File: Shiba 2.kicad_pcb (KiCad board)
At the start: 2 copper layers, 85.7 x 54 mm, 40 parts, among them J1 Conn_01x04_Pin, U1 STM32F072C8Tx, U3 AP62150Z6, U5 MIC5504-3.3YM5

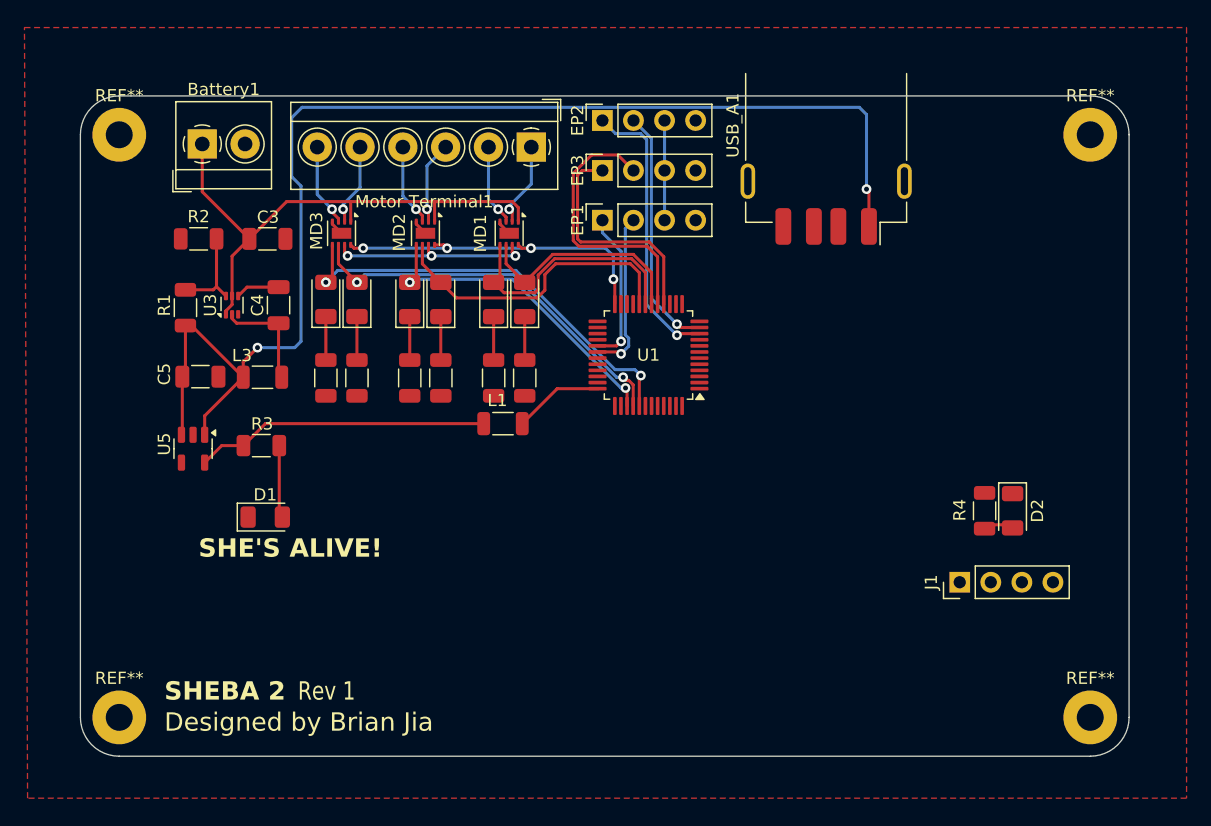
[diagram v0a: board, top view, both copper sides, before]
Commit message: About ready to order but I realized I used underpowered motor drivers
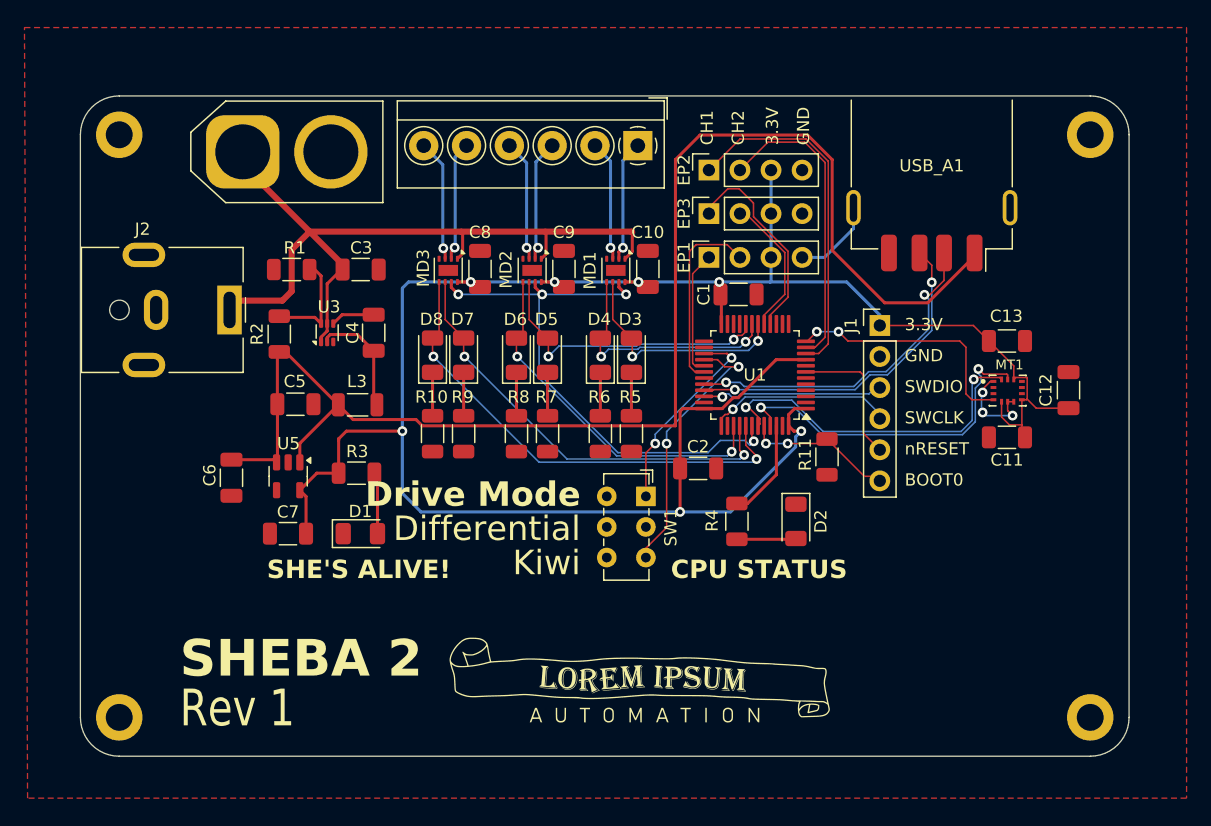
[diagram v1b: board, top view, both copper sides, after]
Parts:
- removed L1: L100nH, Inductor_SMD:L_1206_3216Metric
- removed REF** (x4): MountingHole_2.2mm_M2_Pad, MountingHole:MountingHole_2.2mm_M2_Pad
- added C1: C_Small22uF, Capacitor_SMD:C_1206_3216Metric, F.Cu at (107.1, 46.2)
- added C10: C_Small1uF, Capacitor_SMD:C_1206_3216Metric, F.Cu at (99.7, 44.1)
- added C11: C_Small2.2uF, Capacitor_SMD:C_1206_3216Metric, F.Cu at (129.1, 57.9)
- added C12: C_Small0.1uF, Capacitor_SMD:C_1206_3216Metric, F.Cu at (134.1, 54.0)
- added C13: C_Small10nF, Capacitor_SMD:C_1206_3216Metric, F.Cu at (129.1, 50.0)
- added C2: C_Small22uF, Capacitor_SMD:C_1206_3216Metric, F.Cu at (103.8, 60.4)
- added C6: C1uF, Capacitor_SMD:C_1206_3216Metric, F.Cu at (65.7, 61.2)
- added C7: C1uF, Capacitor_SMD:C_1206_3216Metric, F.Cu at (70.3, 65.8)
- added C8: C_Small1uF, Capacitor_SMD:C_1206_3216Metric, F.Cu at (86.0, 44.1)
- added C9: C_Small1uF, Capacitor_SMD:C_1206_3216Metric, F.Cu at (92.9, 44.1)
- added G***: LOGO, Library:lorem-ipsum-logo, F.Cu at (99.0, 79.9)
- added G***: LOGO, Library:lorem-ipsum-insignia, F.Cu at (124.2, 72.4)
- added H1: MountingHole_Pad, MountingHole:MountingHole_2.2mm_M2_DIN965_Pad, F.Cu at (56.5, 33.1)
- added H2: MountingHole_Pad, MountingHole:MountingHole_2.2mm_M2_DIN965_Pad, F.Cu at (135.9, 33.1)
- added H3: MountingHole_Pad, MountingHole:MountingHole_2.2mm_M2_DIN965_Pad, F.Cu at (56.5, 80.8)
- added H4: MountingHole_Pad, MountingHole:MountingHole_2.2mm_M2_DIN965_Pad, F.Cu at (135.9, 80.8)
- added J2: Jack-DC, Connector_BarrelJack:BarrelJack_CUI_PJ-063AH_Horizontal, F.Cu at (65.5, 47.5)
- added MT1: ICM-42670-P, Library:XDCR_ICM-42670-P, F.Cu at (129.1, 54.1)
- added R11: 10k, Resistor_SMD:R_1206_3216Metric, F.Cu at (114.4, 59.5)
- added SW1: SW_SPDT, Button_Switch_THT:SW_E-Switch_EG1271_SPDT, F.Cu at (99.6, 62.7)
- Battery1: footprint TerminalBlock_4Ucon:TerminalBlock_4Ucon_1x02_P3.50mm_Horizontal -> Connector_AMASS:AMASS_XT60-F_1x02_P7.20mm_Vertical
- C3: value C_Small10uF -> C10uF
- C4: value C_Small100nF -> C0.1uF
- C5: value C_Small22uF -> C22uF
- D1, D2, D3, D5, D7: value LED -> LED Green
- D4, D6, D8: value LED -> LED Red
- J1: value Conn_01x04_Pin -> Conn_01x06_Pin; footprint Connector_PinHeader_2.54mm:PinHeader_1x04_P2.54mm_Vertical -> Connector_PinHeader_2.54mm:PinHeader_1x06_P2.54mm_Vertical
- moved J1 22.0 mm to (118.7, 48.7), turned to 0 degrees
- moved R4 20.3 mm to (107.0, 64.8)
- moved D2 17.7 mm to (111.8, 64.8)
- moved R2 10.2 mm to (69.6, 49.4), turned to 90 degrees
- moved D6 9.84 mm to (89.0, 51.2)
- moved D7 9.84 mm to (84.7, 51.2)
- moved R8 9.84 mm to (89.0, 57.6)
- moved R9 9.84 mm to (84.7, 57.6)
- moved D3 9.84 mm to (98.4, 51.2)
- moved D4 9.84 mm to (95.8, 51.2)
- moved D5 9.84 mm to (91.5, 51.2)
- moved D8 9.84 mm to (82.1, 51.2)
- moved R10 9.84 mm to (82.1, 57.6)
- moved R5 9.84 mm to (98.4, 57.6)
- moved R6 9.84 mm to (95.8, 57.6)
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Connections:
- net SYS_JTCK-SWCLK renamed SYS_SWCLK
- net SYS_JTMS-SWDIO renamed SYS_SWDIO
- R1 pad 2: +5V -> GND
- R2 pad 1: GND -> +5V
- U1 pad 12: unconnected-(U1-PA2-Pad12) -> IMU_INT
- U1 pad 2: M_SLEEP -> unconnected-(U1-PC13-Pad2)
- U1 pad 22: BLINKY -> unconnected-(U1-PB11-Pad22)
- U1 pad 27: unconnected-(U1-PB14-Pad27) -> DIFFERENTIAL_DRIVE
- U1 pad 28: unconnected-(U1-PB15-Pad28) -> KIWI_DRIVE
- U1 pad 36: Net-(U1-VDDA) -> +3V3
- U1 pad 42: unconnected-(U1-PB6-Pad42) -> M_SLEEP
- U1 pad 43: unconnected-(U1-PB7-Pad43) -> I2C1_SDA
- U1 pad 44: GND -> BOOT0
- U1 pad 45: unconnected-(U1-PB8-Pad45) -> IC21_SCL
- U1 pad 46: unconnected-(U1-PB9-Pad46) -> BLINKY
- U1 pad 7: GND -> NRST
- U1 pad 9: Net-(U1-VDDA) -> +3V3
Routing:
- net +3V3: track 60.6 -> 176.1 mm, vias 4 -> 7
- net M_SLEEP: track 16.7 -> 46.3 mm, vias 3 -> 4
- net IC21_SCL: track 0.00 -> 28.5 mm, vias 0 -> 2
- net I2C1_SDA: track 0.00 -> 28.2 mm, vias 0 -> 2
- net /USB_DM: track 0.00 -> 27.8 mm, vias 0 -> 2
- net /USB_DP: track 0.00 -> 27.4 mm, vias 0 -> 2
- net KIWI_DRIVE: track 0.00 -> 21.4 mm, vias 0 -> 2
- net IMU_INT: track 0.00 -> 20.2 mm, vias 0 -> 2
- net +BATT: track 44.2 -> 63.3 mm
- net DIFFERENTIAL_DRIVE: track 0.00 -> 15.9 mm, vias 0 -> 2
- net SYS_SWDIO: track 0.00 -> 15.1 mm, vias 0 -> 1
- net SYS_SWCLK: track 0.00 -> 14.9 mm, vias 0 -> 1
- net BOOT0: track 0.00 -> 12.2 mm, vias 0 -> 2
- net NRST: track 0.00 -> 11.5 mm
- net TIM3_CH2: track 22.9 -> 11.7 mm
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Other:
- board text added: "3.3V"
- board text added: "BOOT0"
- board text added: "CH1"
- board text added: "CH2"
- board text added: "CPU STATUS"
- board text added: "Designed by Brian Jia Wouldn't be possible without: Griffin Bohm Sam Patterson Drew Straub"
- board text added: "Differential"
- board text added: "Drive Mode"
- board text added: "GND"
- board text added: "Kiwi"
- board text added: "SWCLK"
- board text added: "SWDIO"
- board text added: "nRESET"
- board text removed: "Designed by Brian Jia"

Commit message: REV 1 ORDERED WOOOOO
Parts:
- removed C9: C_Small1uF, Capacitor_SMD:C_1206_3216Metric
- added C15: C1uF, Capacitor_SMD:C_1206_3216Metric, F.Cu at (92.0, 46.0)
- added G***: LOGO, LOGO, F.Cu at (103.4, 74.9)
- added J3: Conn_01x010_Pin, Connector_PinSocket_2.54mm:PinSocket_1x10_P2.54mm_Vertical, F.Cu at (135.4, 38.9)
- added R12: R10k, Resistor_SMD:R_1206_3216Metric, F.Cu at (115.1, 65.5)
- added R13: R10k, Resistor_SMD:R_1206_3216Metric, F.Cu at (120.1, 65.5)
- C10, C8: value C_Small1uF -> C1uF
- MD1, MD2, MD3: value DRV8837C -> ZXBM5210-S; footprint Package_SON:WSON-8-1EP_2x2mm_P0.5mm_EP0.9x1.6mm -> Package_SO:SOIC-8_3.9x4.9mm_P1.27mm
- moved MD1 14.8 mm to (82.5, 41.5), turned to 0 degrees
- moved MD3 14.7 mm to (97.9, 41.5), turned to 0 degrees
- moved C12 8.52 mm to (128.8, 60.7), turned to 180 degrees
- moved D2 3.37 mm to (108.5, 64.8)
- moved MD2 2.71 mm to (90.2, 41.5), turned to 0 degrees
- moved G*** 2.51 mm to (126.0, 74.2)
- moved R11 2.31 mm to (112.8, 61.2)
- moved R4 2.10 mm to (104.9, 64.8)
- moved C10 2.05 mm to (98.9, 46.0), turned to 0 degrees
- moved C8 2.05 mm to (85.1, 46.0), turned to 0 degrees
- moved G*** 2.03 mm to (101.1, 79.9)
- moved C1 0.30 mm to (107.4, 46.2)
- moved C13 0.26 mm to (128.8, 50.0)
- moved C11 0.25 mm to (128.8, 57.9)
- renumbered U3 to U1, U5 to U2, U1 to U3
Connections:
- D4 pad 2: M1_BACK -> M1_REV
- D6 pad 2: M2_BACK -> M2_REV
- D8 pad 2: M3_BACK -> M3_REV
- MD1 pad 1: +BATT -> Net-(MD1-OUT1)
- MD1 pad 2: Net-(MD1-OUT1) -> +BATT
- MD1 pad 3: Net-(MD1-OUT2) -> +3V3
- MD1 pad 4: GND -> M3_REV
- MD1 pad 5: M1_BACK -> M3_FWD
- MD1 pad 6: M1_FWD -> +3V3
- MD1 pad 7: M_SLEEP -> Net-(MD1-OUT2)
- MD1 pad 8: +3V3 -> GND
- MD2 pad 1: +BATT -> Net-(MD2-OUT1)
- MD2 pad 2: Net-(MD2-OUT1) -> +BATT
- MD2 pad 3: Net-(MD2-OUT2) -> +3V3
- MD2 pad 4: GND -> M2_REV
- MD2 pad 5: M2_BACK -> M2_FWD
- MD2 pad 6: M2_FWD -> +3V3
- MD2 pad 7: M_SLEEP -> Net-(MD2-OUT2)
- MD2 pad 8: +3V3 -> GND
- MD3 pad 1: +BATT -> Net-(MD3-OUT1)
- MD3 pad 2: Net-(MD3-OUT1) -> +BATT
- MD3 pad 3: Net-(MD3-OUT2) -> +3V3
- MD3 pad 4: GND -> M1_REV
- MD3 pad 5: M3_BACK -> M1_FWD
- MD3 pad 6: M3_FWD -> +3V3
- MD3 pad 7: M_SLEEP -> Net-(MD3-OUT2)
- MD3 pad 8: +3V3 -> GND
- Motor Terminal1 pad 1: Net-(MD1-OUT1) -> Net-(MD3-OUT2)
- Motor Terminal1 pad 2: Net-(MD1-OUT2) -> Net-(MD3-OUT1)
- Motor Terminal1 pad 3: Net-(MD2-OUT1) -> Net-(MD2-OUT2)
- Motor Terminal1 pad 4: Net-(MD2-OUT2) -> Net-(MD2-OUT1)
- Motor Terminal1 pad 5: Net-(MD3-OUT1) -> Net-(MD1-OUT2)
- Motor Terminal1 pad 6: Net-(MD3-OUT2) -> Net-(MD1-OUT1)
- U3 pad 13: unconnected-(U1-PA3-Pad13) -> GPIO_5
- U3 pad 14: unconnected-(U1-PA4-Pad14) -> GPIO_6
- U3 pad 15: unconnected-(U1-PA5-Pad15) -> GPIO_7
- U3 pad 19: M1_BACK -> M1_REV
- U3 pad 2: unconnected-(U1-PC13-Pad2) -> GPIO_0
- U3 pad 3: unconnected-(U1-PC14-Pad3) -> GPIO_1
- U3 pad 39: M2_BACK -> M2_REV
- U3 pad 4: unconnected-(U1-PC15-Pad4) -> GPIO_2
- U3 pad 41: M3_BACK -> M3_REV
- U3 pad 42: M_SLEEP -> unconnected-(U3-PB6-Pad42)
- U3 pad 5: unconnected-(U1-PF0-Pad5) -> GPIO_3
- U3 pad 6: unconnected-(U1-PF1-Pad6) -> GPIO_4
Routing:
- net +3V3: track 176.1 -> 243.3 mm
- net M_SLEEP: track 46.3 -> 0.00 mm, vias 4 -> 0
- net GPIO_4: track 0.00 -> 44.5 mm
- net GPIO_3: track 0.00 -> 42.1 mm
- net M3_REV: track 0.00 -> 41.9 mm, vias 0 -> 2
- net GPIO_2: track 0.00 -> 39.8 mm
- net M3_BACK: track 39.5 -> 0.00 mm, vias 2 -> 0
- net GPIO_1: track 0.00 -> 38.1 mm, vias 0 -> 1
- net GPIO_0: track 0.00 -> 35.5 mm, vias 0 -> 1
- net GPIO_7: track 0.00 -> 32.3 mm, vias 0 -> 2
- net M2_REV: track 0.00 -> 31.7 mm, vias 0 -> 2
- net M2_BACK: track 29.5 -> 0.00 mm, vias 2 -> 0
- net GPIO_6: track 0.00 -> 29.2 mm, vias 0 -> 2
- net GPIO_5: track 0.00 -> 26.1 mm, vias 0 -> 2
- net M1_REV: track 0.00 -> 22.2 mm, vias 0 -> 2
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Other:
- board text added: "0"
- board text added: "1"
- board text added: "2"
- board text added: "3"
- board text added: "4"
- board text added: "5"
- board text added: "6"
- board text added: "7"
- board text added: "GPIO"

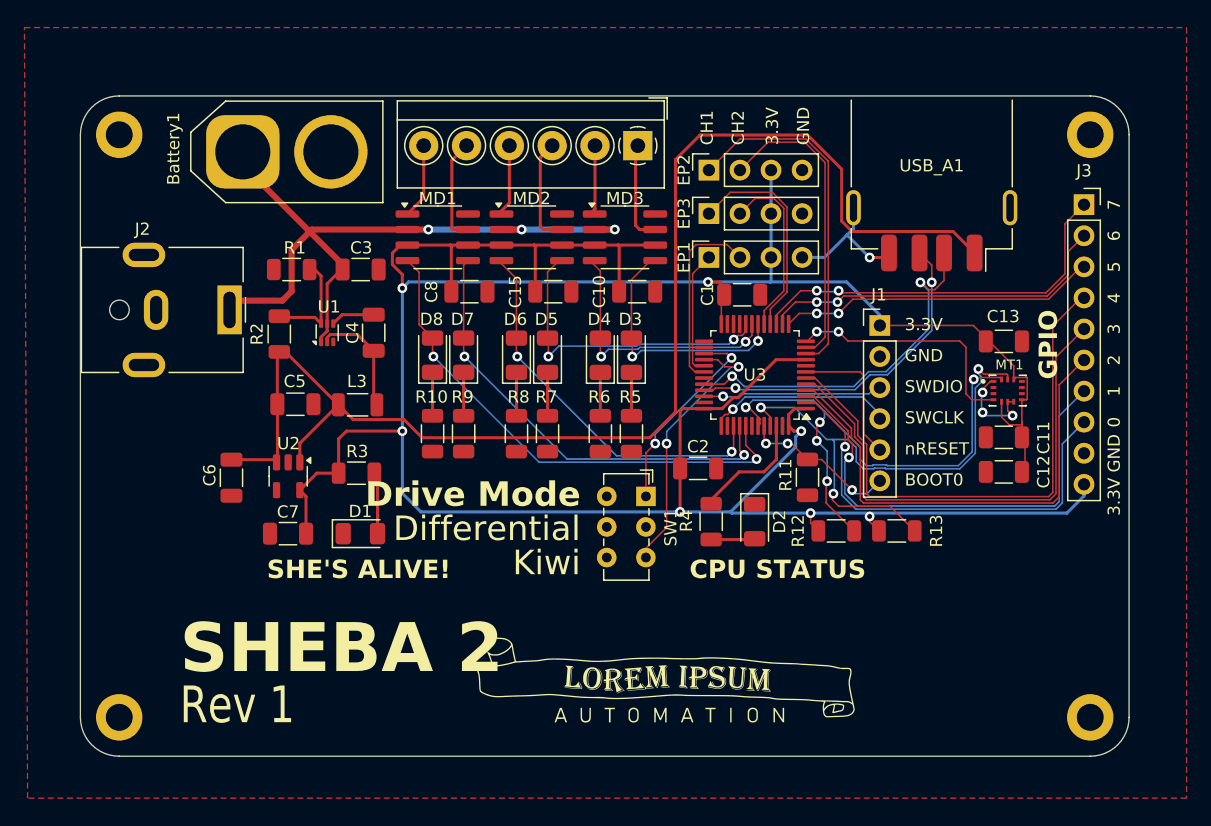
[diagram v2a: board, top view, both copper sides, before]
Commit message: going to prepare BOM for Rev 1 order
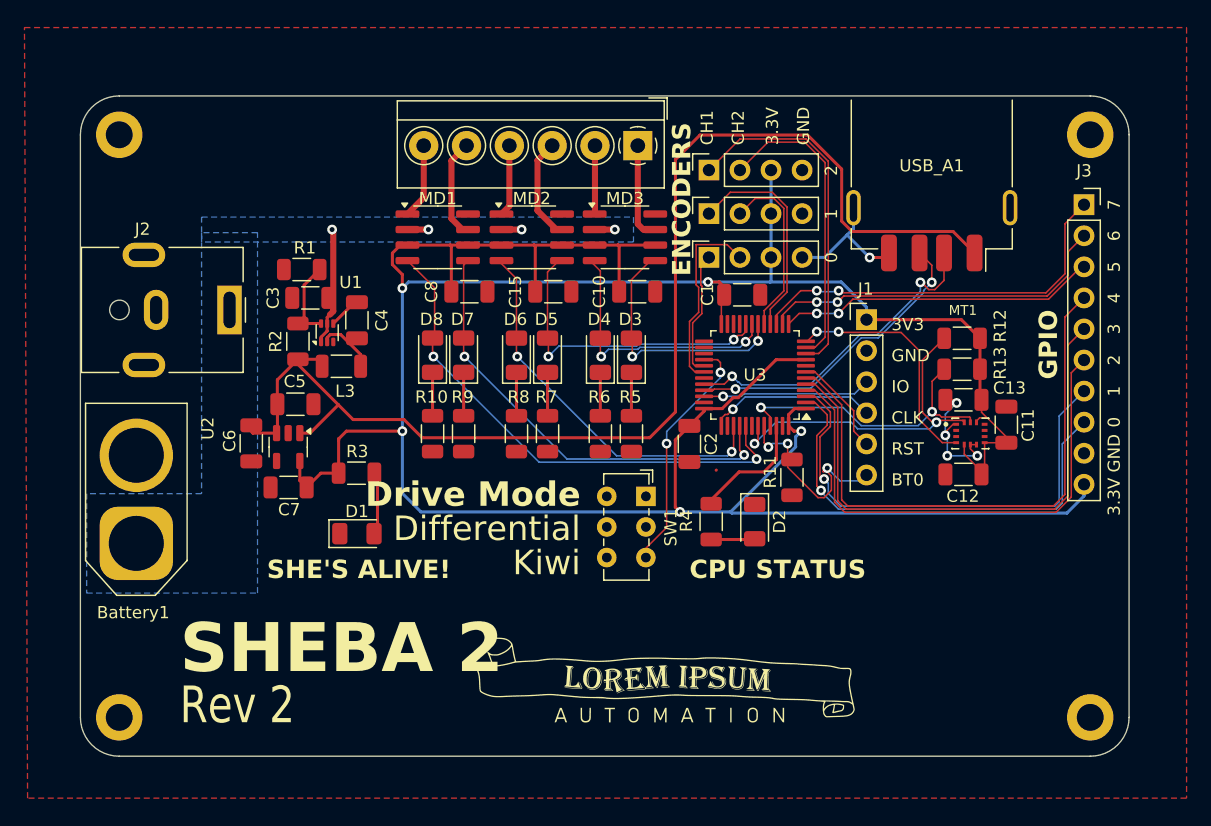
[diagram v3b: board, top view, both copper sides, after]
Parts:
- moved Battery1 33.2 mm to (57.9, 66.5), turned to 90 degrees
- moved R12 18.8 mm to (125.4, 49.8), turned to 0 degrees
- moved R13 14.3 mm to (125.4, 52.3), turned to 0 degrees
- moved C13 5.81 mm to (125.5, 54.8), turned to 180 degrees
- moved C3 4.72 mm to (72.1, 46.5), turned to 180 degrees
- moved MT1 4.65 mm to (126.1, 57.6)
- moved C7 3.78 mm to (70.4, 62.0)
- moved L3 3.42 mm to (74.7, 52.1)
- moved C12 3.31 mm to (125.5, 60.9)
- moved C6 3.25 mm to (67.3, 58.4)
- moved U2 2.39 mm to (70.3, 58.7)
- moved C2 2.12 mm to (103.1, 58.4), turned to -90 degrees
- moved C4 1.71 mm to (75.9, 48.3)
- moved R2 1.64 mm to (71.1, 50.0)
- moved R11 1.27 mm to (111.5, 61.2)
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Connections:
- SW1 pad 1: DIFFERENTIAL_DRIVE -> unconnected-(SW1-A-Pad1)
- U3 pad 27: DIFFERENTIAL_DRIVE -> unconnected-(U3-PB14-Pad27)
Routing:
- net +BATT: track 57.9 -> 14.7 mm, vias 3 -> 4
- net IC21_SCL: track 45.9 -> 24.6 mm, vias 3 -> 2
- net DIFFERENTIAL_DRIVE: track 15.9 -> 0.00 mm, vias 2 -> 0
- net I2C1_SDA: track 44.0 -> 28.3 mm, vias 5 -> 2
- net +5V: track 107.5 -> 101.6 mm
- net +3V3: track 243.3 -> 238.4 mm, vias 7 -> 5
- net Net-(U1-SW): track 9.33 -> 4.83 mm
- net GND: track 18.8 -> 22.5 mm, vias 4 -> 5
- net BOOT0: track 12.9 -> 16.6 mm
- net NRST: track 11.5 -> 8.37 mm
- net /USB_DM: track 29.9 -> 27.0 mm
- net GPIO_3: track 42.1 -> 44.8 mm
- net GPIO_4: track 44.5 -> 47.2 mm
- net GPIO_2: track 39.8 -> 42.4 mm
- net /USB_DP: track 27.5 -> 25.2 mm
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- added copper zone on B.Cu, net +BATT
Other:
- board text added: "3V3"
- board text added: "BT0"
- board text added: "CLK"
- board text added: "ENCODERS"
- board text added: "IO"
- board text added: "RST"
- board text added: "Rev 2"
- board text removed: "BOOT0"
- board text removed: "Rev 1"
- board text removed: "SWCLK"
- board text removed: "SWDIO"
- board text removed: "nRESET"

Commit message: Rev 1 BOM ordered let's goooooo!
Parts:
- C1, C2: value C_Small22uF -> C1uF; footprint Capacitor_SMD:C_1206_3216Metric -> Capacitor_SMD:C_1206_3216Metric_Pad1.33x1.80mm_HandSolder
- C10, C15, C3, C4, C5, C6, C7, C8: footprint Capacitor_SMD:C_1206_3216Metric -> Capacitor_SMD:C_1206_3216Metric_Pad1.33x1.80mm_HandSolder
- C11: value C_Small2.2uF -> C2.2uF; footprint Capacitor_SMD:C_1206_3216Metric -> Capacitor_SMD:C_1206_3216Metric_Pad1.33x1.80mm_HandSolder
- C12: value C_Small0.1uF -> C0.1uF; footprint Capacitor_SMD:C_1206_3216Metric -> Capacitor_SMD:C_1206_3216Metric_Pad1.33x1.80mm_HandSolder
- C13: value C_Small10nF -> C0.01uF; footprint Capacitor_SMD:C_1206_3216Metric -> Capacitor_SMD:C_1206_3216Metric_Pad1.33x1.80mm_HandSolder
- D1, D2, D3, D4, D5, D6, D7, D8: footprint LED_SMD:LED_1206_3216Metric -> LED_SMD:LED_1206_3216Metric_Pad1.42x1.75mm_HandSolder
- R1, R10, R12, R13, R2, R3, R4, R5, R6, R7, R8, R9: footprint Resistor_SMD:R_1206_3216Metric -> Resistor_SMD:R_1206_3216Metric_Pad1.30x1.75mm_HandSolder
- R11: value 10k -> R10k; footprint Resistor_SMD:R_1206_3216Metric -> Resistor_SMD:R_1206_3216Metric_Pad1.30x1.75mm_HandSolder
- moved C6 0.25 mm to (67.1, 58.4)
- moved C3 0.25 mm to (72.1, 46.2)
- moved C7 0.25 mm to (70.4, 62.2)
- moved C11 0.25 mm to (129.3, 56.8)
- moved R1 0.22 mm to (71.4, 43.9)
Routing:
- net IC21_SCL: track 24.6 -> 23.8 mm
